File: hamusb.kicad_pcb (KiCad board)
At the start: 2 copper layers, 37.5 x 17.5 mm, 20 parts, among them P1 USB, P2 DATA, Q1 2N7002E, U1 FT232RL, U2 74AC125, Y1 12MHz

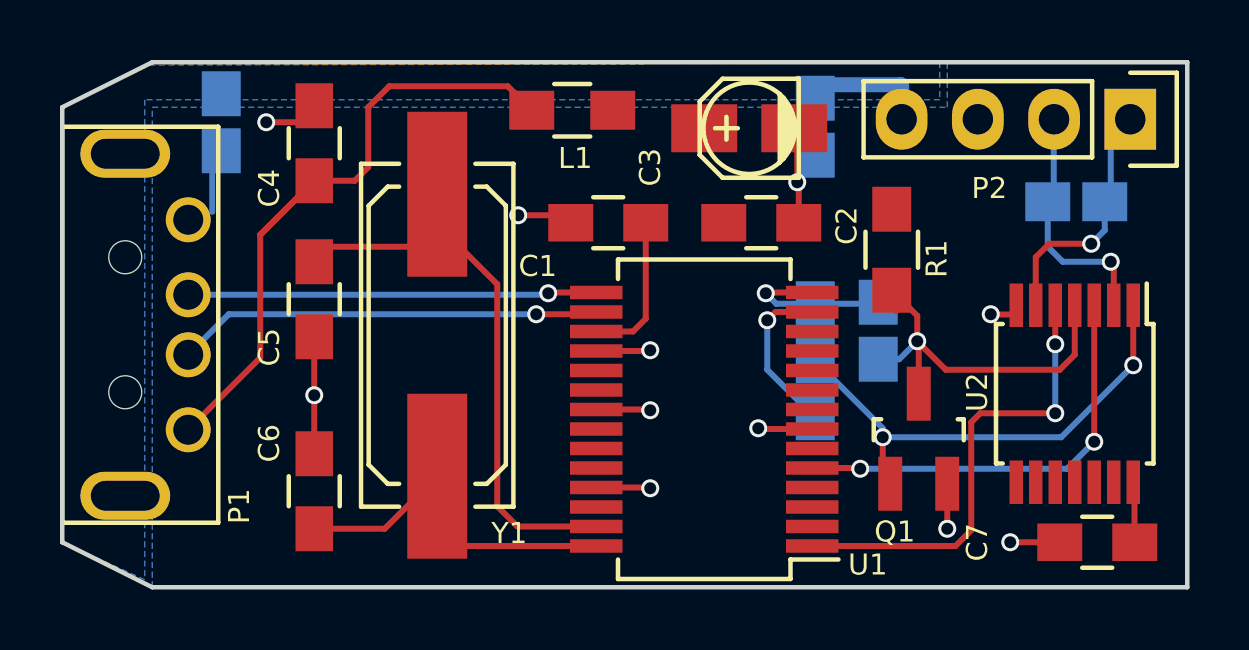
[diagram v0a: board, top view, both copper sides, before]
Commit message: Cleanup, swapped logic gates, reordered input power circuit
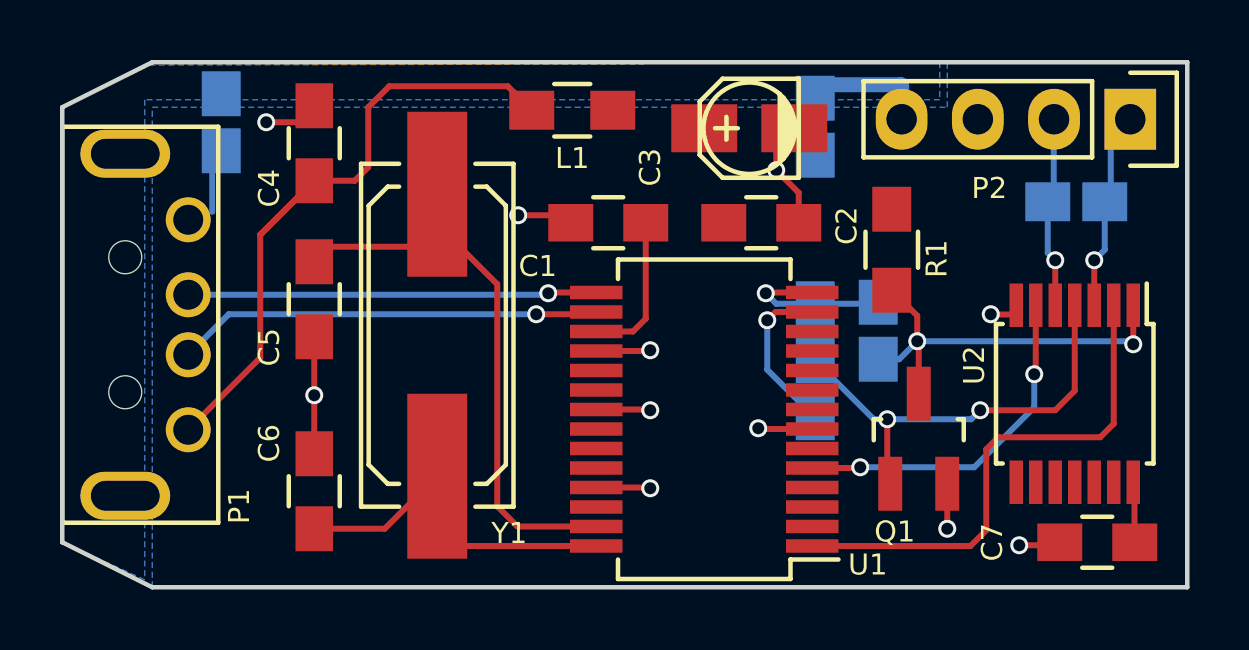
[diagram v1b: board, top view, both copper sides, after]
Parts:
- P1: footprint USB_A_M -> onitake:USB_A_M
- turned L1 to 0 degrees
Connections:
- L1 pad 1: VCC -> Net-(C4-Pad1)
- L1 pad 2: Net-(C4-Pad1) -> VCC
- U2 pad 1: Net-(JP2-Pad2) -> Net-(JP4-Pad2)
- U2 pad 2: Net-(JP1-Pad2) -> Net-(U1-Pad1)
- U2 pad 3: Net-(U1-Pad5) -> Net-(JP1-Pad1)
- U2 pad 4: Net-(JP4-Pad2) -> Net-(JP2-Pad2)
- U2 pad 5: Net-(U1-Pad1) -> Net-(JP1-Pad2)
- U2 pad 6: Net-(JP1-Pad1) -> Net-(U1-Pad5)
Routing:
- net Net-(U1-Pad5): track 14.3 -> 11.7 mm
- net Net-(JP1-Pad2): track 8.48 -> 6.79 mm
- net Net-(JP1-Pad1): track 8.67 -> 7.04 mm
- net Net-(U1-Pad1): track 15.7 -> 17.3 mm, vias 2 -> 0
- net Net-(JP2-Pad2): track 16.5 -> 15.2 mm
- net Net-(JP4-Pad2): track 13.6 -> 13.9 mm, vias 1 -> 2

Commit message: Added additional net labels Increased shield copper area
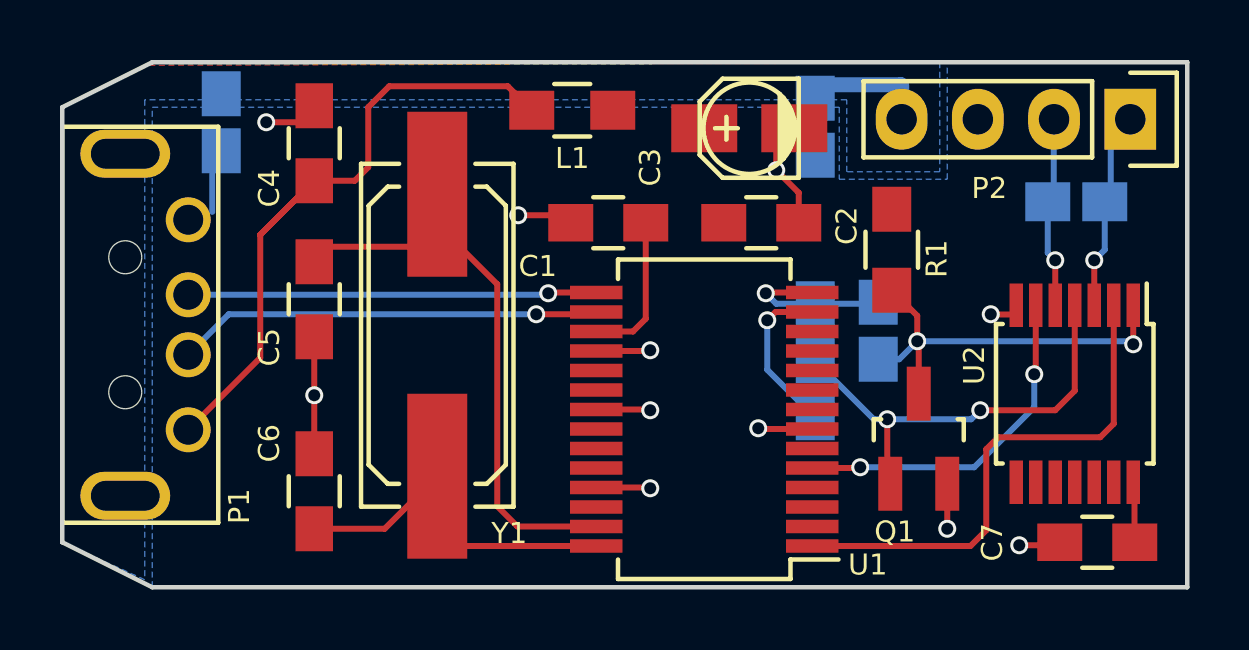
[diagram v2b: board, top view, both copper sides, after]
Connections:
- net Net-(JP1-Pad1) renamed /DO
- net Net-(JP1-Pad2) renamed /DI
- net Net-(P1-Pad2) renamed /D-
- net Net-(P1-Pad3) renamed /D+
- net Net-(U1-Pad1) renamed /TX
- net Net-(U1-Pad5) renamed /RX
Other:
- net class Earth removed

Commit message: Simplified shield plane Minor placement cleanups
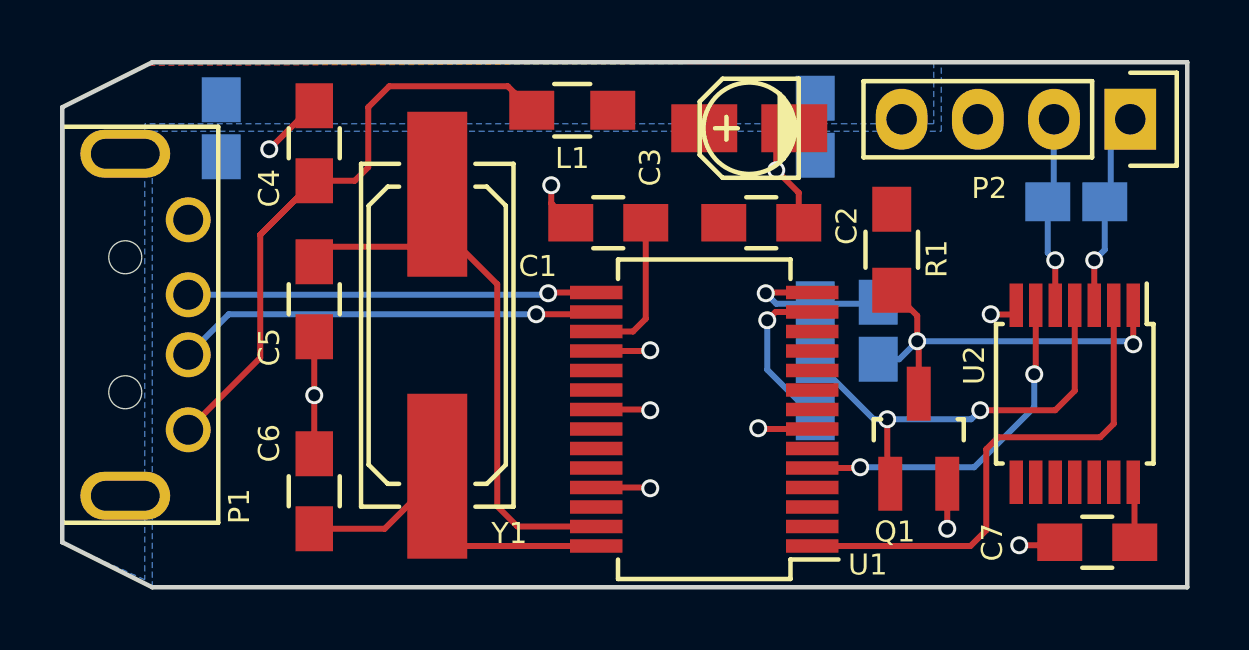
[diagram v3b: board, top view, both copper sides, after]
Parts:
- moved JP3 0.20 mm to (131.8, 99.2)
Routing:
- net Earth: track 4.20 -> 0.00 mm
- net GND: track 24.2 -> 23.3 mm
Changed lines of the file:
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@@
     (links 50)
     (no_connects 0)
-    (area 110.624999 91.15 175 114.575001)
+    (area 126.424999 96.924999 164.075001 114.575001)
     (thickness 1.6)
     (drawings 8)
-    (tracks 150)
+    (tracks 147)
     (zones 0)
     (modules 20)
@@
   (title_block
     (title "Ham Radio USB Data Programmer")
-    (date 2015-10-27)
-    (rev 5)
+    (date 2015-10-28)
+    (rev 6)
     (company "© 2015 Gregor Riepl")
     (comment 1 "Licensed under the CERN OHL v1.2")
@@
   )
   (layers
-    (0 F.Cu signal hide)
+    (0 F.Cu signal)
     (31 B.Cu signal)
     (32 B.Adhes user)
@@
     (tags "resistor 0805")
     (attr smd)
-    (fp_text reference JP1 (at 1 -1.6 360) (layer B.SilkS)
+    (fp_text reference JP1 (at -2.6 -0.05 450) (layer B.SilkS)
       (effects (font (size 0.7 0.7) (thickness 0.15)) (justify mirror))
     )
@@
   )
   (module onitake:Jumper_SMD_2Pin (layer B.Cu)
-    (at 131.8 99 90)
+    (at 131.8 99.2 90)
     (descr "2 contact SMD solder pad")
     (tags "solder pad jumper")
     (attr smd)
-    (fp_text reference JP3 (at 1.2 1.9 180) (layer B.SilkS)
+    (fp_text reference JP3 (at 0.9 1.7 270) (layer B.SilkS)
       (effects (font (size 0.7 0.7) (thickness 0.15)) (justify mirror))
     )
@@
   (segment (start 145.525 105.975) (end 144.525 105.975) (width 0.2) (layer F.Cu) (net 1))
   (segment (start 145.95 105.55) (end 145.525 105.975) (width 0.2) (layer F.Cu) (net 1))
-  (segment (start 154.48 98.9) (end 154.48 97.77) (width 0.5) (layer B.Cu) (net 2))
-  (segment (start 154.46 97.75) (end 152.05 97.75) (width 0.5) (layer B.Cu) (net 2))
-  (segment (start 154.48 97.77) (end 154.46 97.75) (width 0.5) (layer B.Cu) (net 2))
-  (segment (start 152.05 97.75) (end 151.6 98.2) (width 0.5) (layer B.Cu) (net 2))
   (segment (start 162.2431 110.994) (end 162.2431 112.9931) (width 0.2) (layer F.Cu) (net 3))
   (segment (start 162.2431 112.9931) (end 162.25 113) (width 0.2) (layer F.Cu) (net 3))
@@
   (segment (start 154 110.95114) (end 154.1 111.05114) (width 0.2) (layer F.Cu) (net 9))
   (segment (start 154.1 111.05114) (end 153.85 110.80114) (width 0.2) (layer F.Cu) (net 9))
+  (segment (start 143.45 102.35) (end 142.8 101.7) (width 0.2) (layer F.Cu) (net 10))
+  (via (at 142.8 101.1) (size 0.6) (drill 0.4) (layers F.Cu B.Cu) (net 10))
+  (segment (start 142.8 101.7) (end 142.8 101.1) (width 0.2) (layer F.Cu) (net 10))
+  (segment (start 134.9 98.45) (end 134.85 98.45) (width 0.2) (layer F.Cu) (net 10))
+  (segment (start 134.85 98.45) (end 133.4 99.9) (width 0.2) (layer F.Cu) (net 10))
+  (via (at 133.4 99.9) (size 0.6) (drill 0.4) (layers F.Cu B.Cu) (net 10))
   (segment (start 151.05 102.35) (end 151.05 101.35) (width 0.2) (layer F.Cu) (net 10))
   (via (at 150.3 100.6) (size 0.6) (drill 0.4) (layers F.Cu B.Cu) (net 10))
@@
   (segment (start 159.65 113.1) (end 158.4 113.1) (width 0.2) (layer F.Cu) (net 10))
   (via (at 158.4 113.1) (size 0.6) (drill 0.4) (layers F.Cu B.Cu) (net 10))
-  (segment (start 131.50212 101.98714) (end 131.50212 100.24788) (width 0.2) (layer B.Cu) (net 10))
   (segment (start 131.50212 100.24788) (end 131.8 99.95) (width 0.2) (layer B.Cu) (net 10))
   (segment (start 156 111.05114) (end 156 112.55) (width 0.2) (layer F.Cu) (net 10))
@@
   (segment (start 146.075 106.625) (end 146.1 106.6) (width 0.2) (layer F.Cu) (net 10))
   (segment (start 134.9 98.45) (end 134.35 99) (width 0.2) (layer F.Cu) (net 10))
-  (segment (start 134.35 99) (end 133.3 99) (width 0.2) (layer F.Cu) (net 10))
-  (via (at 133.3 99) (size 0.6) (drill 0.4) (layers F.Cu B.Cu) (net 10))
   (segment (start 134.9 110.05) (end 134.9 108.1) (width 0.2) (layer F.Cu) (net 10))
   (via (at 134.9 108.1) (size 0.6) (drill 0.4) (layers F.Cu B.Cu) (net 10))
@@
   (segment (start 151.05 99.34886) (end 150.90114 99.2) (width 0.2) (layer F.Cu) (net 10))
   (segment (start 134.9 109.41286) (end 134.9 109.4) (width 0.2) (layer F.Cu) (net 10))
-  (segment (start 143.45 102.1) (end 141.7 102.1) (width 0.2) (layer F.Cu) (net 10))
-  (via (at 141.7 102.1) (size 0.6) (drill 0.4) (layers F.Cu B.Cu) (net 10))
   (segment (start 151.15 98.84886) (end 150.90114 98.6) (width 0.2) (layer F.Cu) (net 10))
   (segment (start 162.2 105.1) (end 162.2 106.4) (width 0.2) (layer F.Cu) (net 11))
@@
     (polygon
       (pts
-        (xy 164 114.5) (xy 129.5 114.5) (xy 129.5 98.5) (xy 152.4 98.5) (xy 152.4 100.9)
-        (xy 156 100.9) (xy 156 97) (xy 164 97) (xy 164 114.5)
+        (xy 164 114.5) (xy 129.5 114.5) (xy 129.5 99.3) (xy 155.8 99.3) (xy 155.8 97)
+        (xy 164 97) (xy 164 114.5)
       )
     )
@@
     (polygon
       (pts
-        (xy 155.75 97) (xy 155.75 100.65) (xy 152.65 100.65) (xy 152.65 98.25) (xy 129.25 98.25)
+        (xy 155.55 97) (xy 155.55 99.05) (xy 152.65 99.05) (xy 152.65 99.05) (xy 129.25 99.05)
         (xy 129.25 114.25) (xy 126.5 113) (xy 126.5 98.5) (xy 129.5 97)
       )
